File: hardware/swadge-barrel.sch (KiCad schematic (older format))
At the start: 45 parts, among them J1 USB_B_Micro, Q1 Q_NPN_BEC, SW4 SW_SPDT, U1 ESP-13-WROOM-02D, U2 DISP_OLED_UG-2864HSWEG01, U3 BUS_PCIexpress, U4 QMA6981, U5 AP1117-33

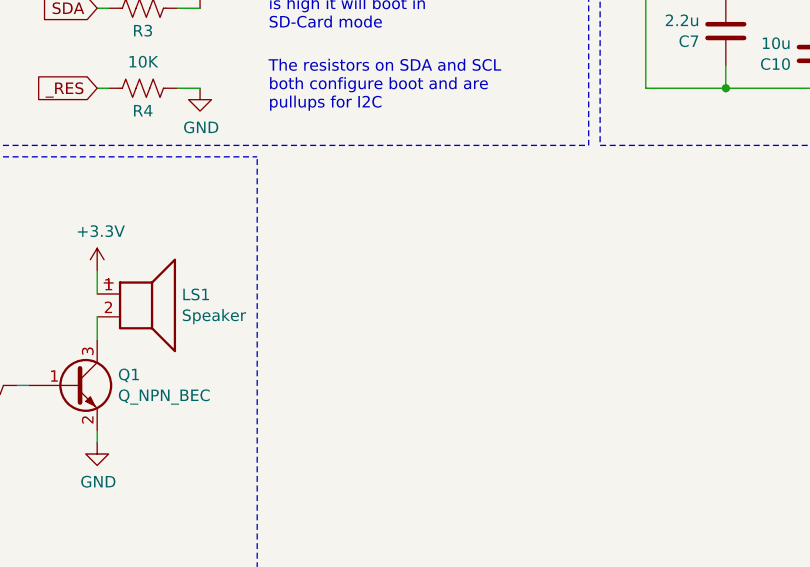
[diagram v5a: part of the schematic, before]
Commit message: Added 0ohm support resistors
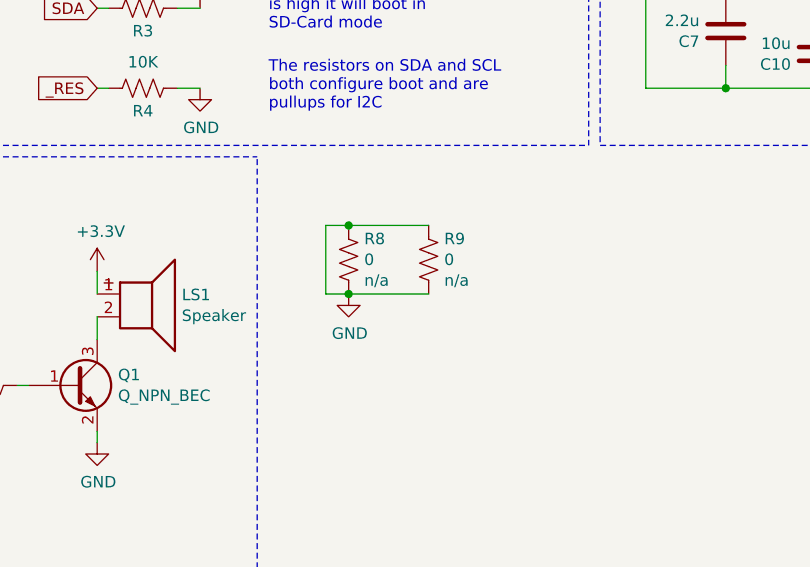
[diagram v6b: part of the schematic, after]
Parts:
- added R8, R9: 0, Swadge_Parts:R_0603_1608Metric, symbol Swadge_Parts:R_US
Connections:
- net GND: now also R8.1, R8.2, R9.1, R9.2
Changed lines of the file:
@@
 Wire Notes Line
 	500  7750 2200 7750
+$Comp
+L Swadge_Parts:R_US R8
+U 1 1 5D6E1A5B
+P 2600 6400
+F 0 "R8" H 2668 6491 50  0000 L CNN
+F 1 "0" H 2668 6400 50  0000 L CNN
+F 2 "Swadge_Parts:R_0603_1608Metric" V 2640 6390 50  0001 C CNN
+F 3 "~" V 2700 6400 50  0001 C CNN
+F 4 "n/a" H 2668 6309 50  0000 L CNN "Digikey"
+F 5 "10" H 2600 6400 10  0001 C CNN "Cost100"
+F 6 "Y" H 2600 6400 10  0001 C CNN "Substitutable"
+	1    2600 6400
+	1    0    0    -1
+$EndComp
+$Comp
+L Swadge_Parts:R_US R9
+U 1 1 5D6E3BEA
+P 2950 6400
+F 0 "R9" H 3018 6491 50  0000 L CNN
+F 1 "0" H 3018 6400 50  0000 L CNN
+F 2 "Swadge_Parts:R_0603_1608Metric" V 2990 6390 50  0001 C CNN
+F 3 "~" V 3050 6400 50  0001 C CNN
+F 4 "n/a" H 3018 6309 50  0000 L CNN "Digikey"
+F 5 "10" H 2950 6400 10  0001 C CNN "Cost100"
+F 6 "Y" H 2950 6400 10  0001 C CNN "Substitutable"
+	1    2950 6400
+	1    0    0    -1
+$EndComp
+Wire Wire Line
+	2950 6250 2600 6250
+Wire Wire Line
+	2950 6550 2600 6550
+Wire Wire Line
+	2600 6550 2500 6550
+Wire Wire Line
+	2500 6550 2500 6250
+Wire Wire Line
+	2500 6250 2600 6250
+Connection ~ 2600 6550
+Connection ~ 2600 6250
+$Comp
+L power:GND #PWR049
+U 1 1 5D712417
+P 2600 6550
+F 0 "#PWR049" H 2600 6300 50  0001 C CNN
+F 1 "GND" H 2605 6377 50  0000 C CNN
+F 2 "" H 2600 6550 50  0001 C CNN
+F 3 "" H 2600 6550 50  0001 C CNN
+	1    2600 6550
+	1    0    0    -1
+$EndComp
 $EndSCHEMATC

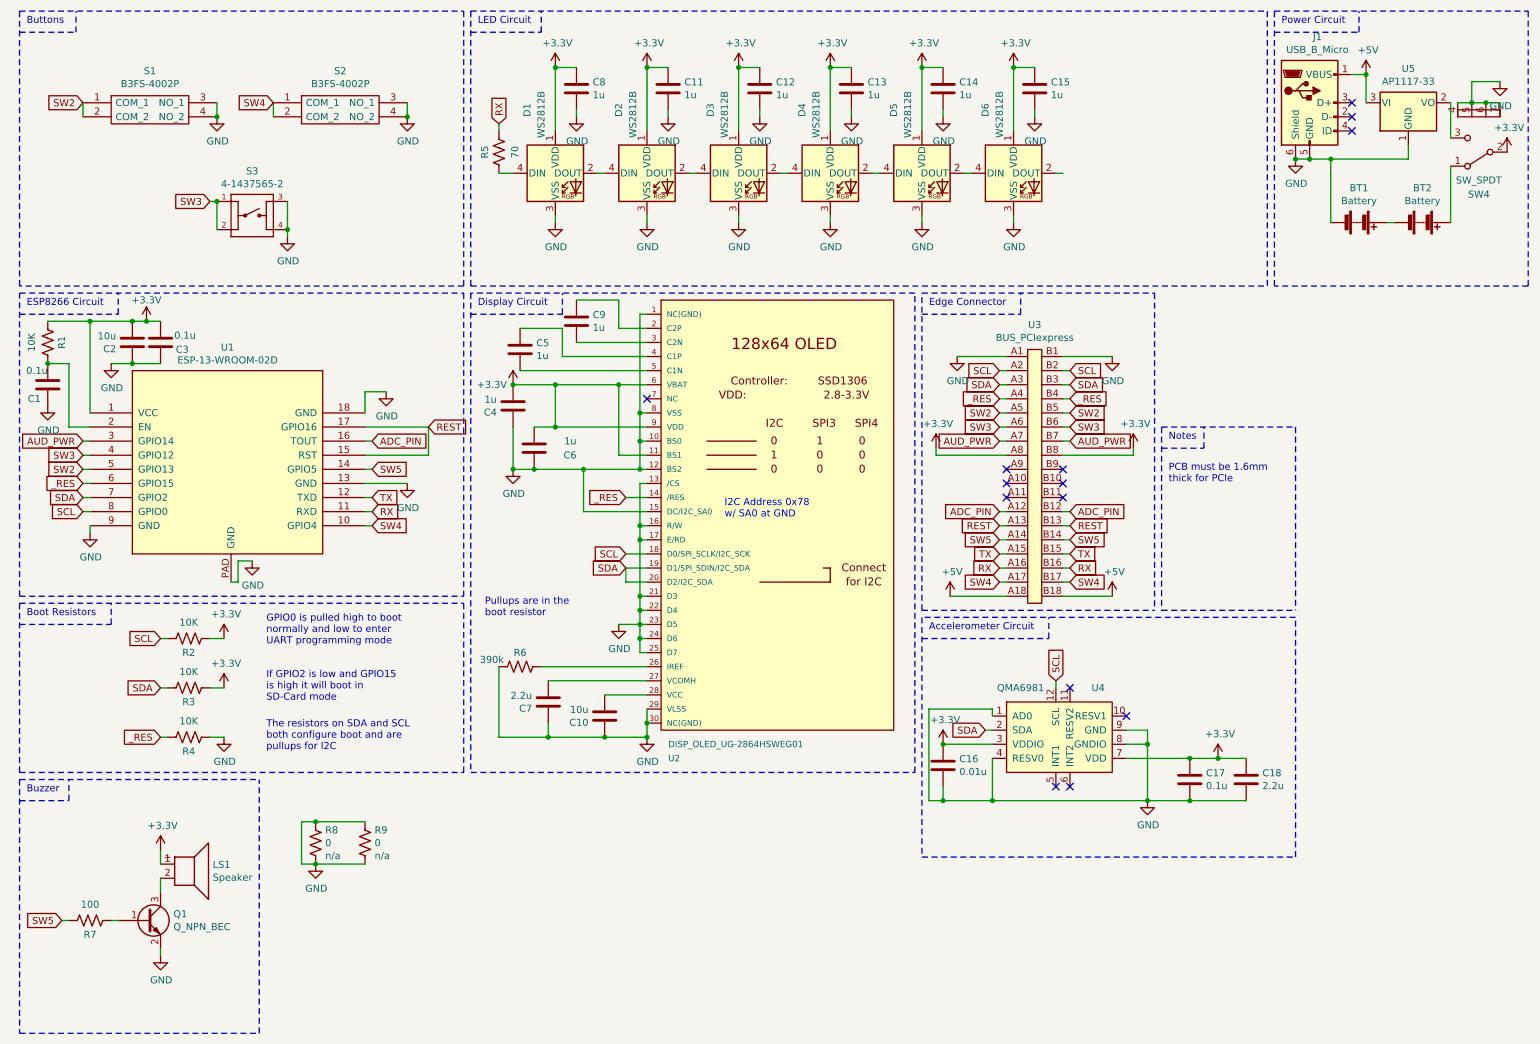
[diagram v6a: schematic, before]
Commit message: #21 added LED OUT to PCIe connector
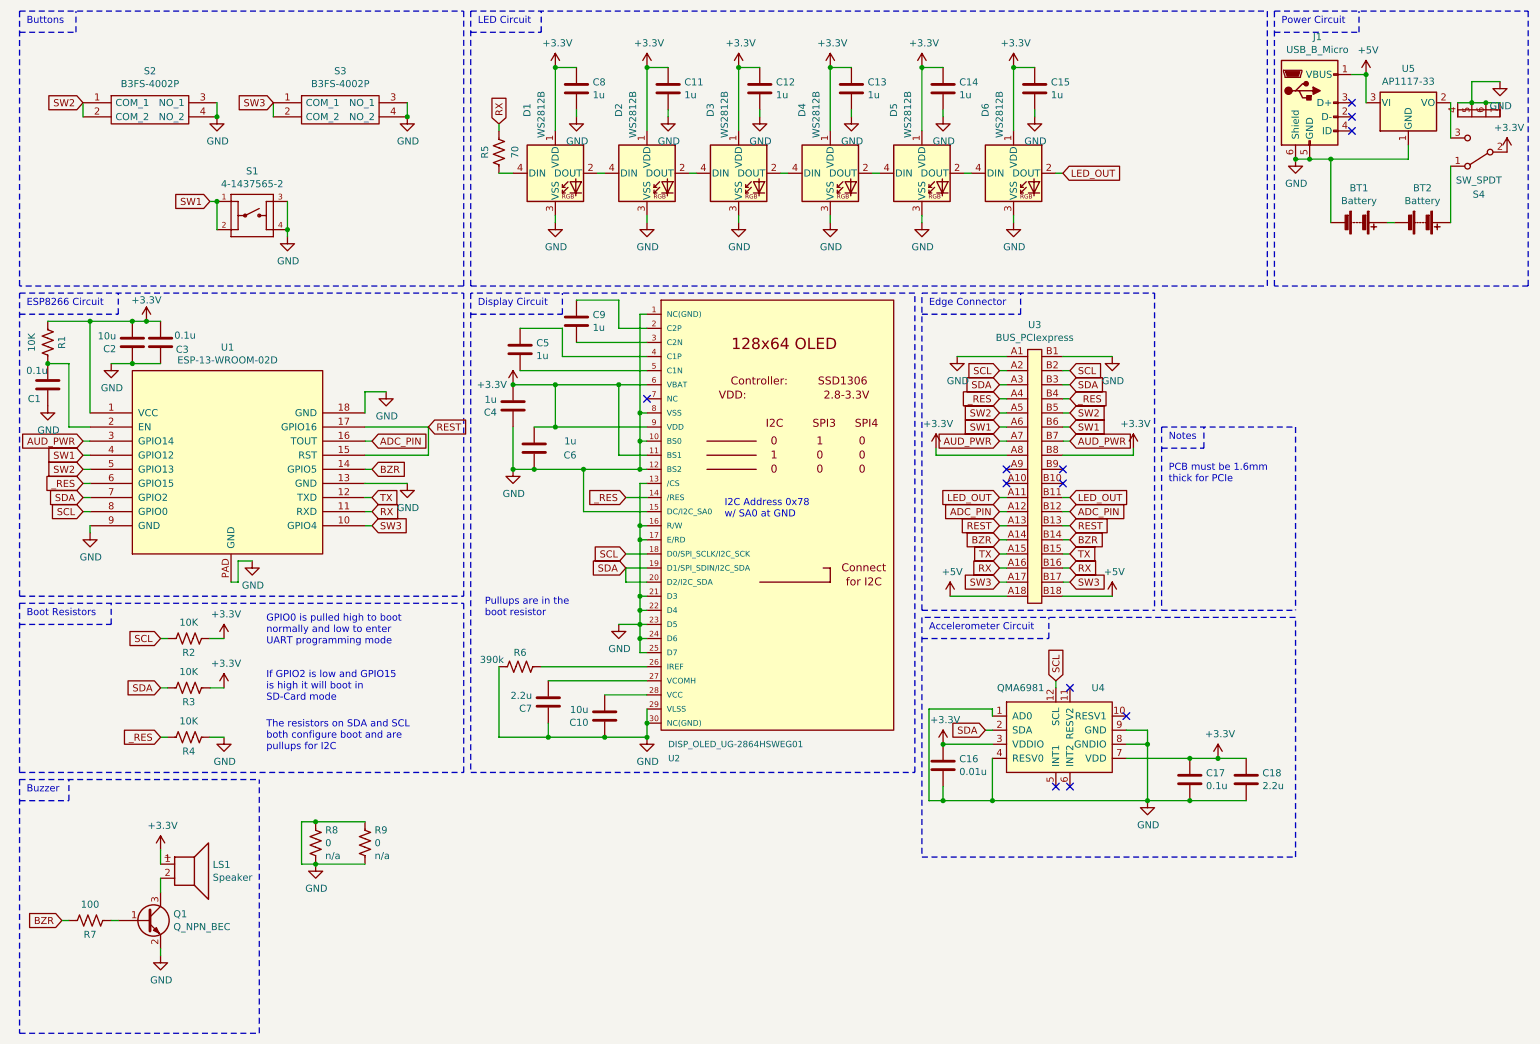
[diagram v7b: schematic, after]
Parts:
- renumbered S3 to S1, S1 to S2, S2 to S3, SW4 to S4
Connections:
- net SW4 is gone; now on net SW3: S3.1 (COM_1), S3.2 (COM_2), U1.10 (GPIO4), U3.A17, U3.B17
- net SW3: no longer S1.1, S1.2, U1.4 (GPIO12), U3.A6, U3.B6
- net LED_OUT: now reaches D6.2 (DOUT)
- net LED_OUT: now also U3.A11, U3.B11
- net SW5 renamed BZR
- new net SW1: S1.1, S1.2, U1.4 (GPIO12), U3.A6, U3.B6
- no-connect marks 14 -> 12

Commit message: Replaced 0805 caps with 1206 caps
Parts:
- C4, C5, C6, C9: footprint Swadge_Parts:C_0805_2012Metric -> Swadge_Parts:C_1206_3216Metric
- U2: footprint Swadge_Parts:oled-flat -> Swadge_Parts:oled-flat_copy
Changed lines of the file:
@@
 F 0 "U2" H 5100 2300 45  0000 L CNN
 F 1 "DISP_OLED_UG-2864HSWEG01" H 5100 2400 45  0000 L CNN
-F 2 "Swadge_Parts:oled-flat" H 5980 4200 20  0001 C CNN
+F 2 "Swadge_Parts:oled-flat_copy" H 5980 4200 20  0001 C CNN
 F 3 "http://www.vishay.com/docs/37903/oled128o064dgpp3n00000.pdf" H 5950 4050 50  0001 C CNN
 F 4 "988" H 0   0   50  0001 C CNN "Cost100"
@@
 F 0 "C6" H 3850 3650 50  0000 L CNN
 F 1 "1u" H 3850 3550 50  0000 L CNN
-F 2 "Swadge_Parts:C_0805_2012Metric" H 4188 3450 50  0001 C CNN
+F 2 "Swadge_Parts:C_1206_3216Metric" H 4188 3450 50  0001 C CNN
 F 3 "" H 4150 3600 50  0001 C CNN
 F 4 "10" H 0   0   50  0001 C CNN "Cost100"
@@
 F 0 "C4" H 4115 3346 50  0000 L CNN
 F 1 "1u" H 4115 3255 50  0000 L CNN
-F 2 "Swadge_Parts:C_0805_2012Metric" H 4038 3150 50  0001 C CNN
+F 2 "Swadge_Parts:C_1206_3216Metric" H 4038 3150 50  0001 C CNN
 F 3 "" H 4000 3300 50  0001 C CNN
 F 4 "10" H 0   0   50  0001 C CNN "Cost100"
@@
 F 0 "C9" H 4565 2746 50  0000 L CNN
 F 1 "1u" H 4565 2655 50  0000 L CNN
-F 2 "Swadge_Parts:C_0805_2012Metric" H 4488 2550 50  0001 C CNN
+F 2 "Swadge_Parts:C_1206_3216Metric" H 4488 2550 50  0001 C CNN
 F 3 "" H 4450 2700 50  0001 C CNN
 F 4 "10" H 0   0   50  0001 C CNN "Cost100"
@@
 F 0 "C5" H 4165 2946 50  0000 L CNN
 F 1 "1u" H 4165 2855 50  0000 L CNN
-F 2 "Swadge_Parts:C_0805_2012Metric" H 4088 2750 50  0001 C CNN
+F 2 "Swadge_Parts:C_1206_3216Metric" H 4088 2750 50  0001 C CNN
 F 3 "" H 4050 2900 50  0001 C CNN
 F 4 "10" H 0   0   50  0001 C CNN "Cost100"
